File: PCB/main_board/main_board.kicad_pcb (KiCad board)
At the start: 4 copper layers, 57 x 29 mm, 55 parts, among them CN1 XT30PW-M, CN2 XT30PW-M, U1 XT30PW-F, U2 W25Q32JVUUIQ, U3 W25N01GVZEIG_C907680, U4 INA226, U5 INA226, U6 RP2040, U7 AZ1117-3.3, X1 X322512MSB4SI

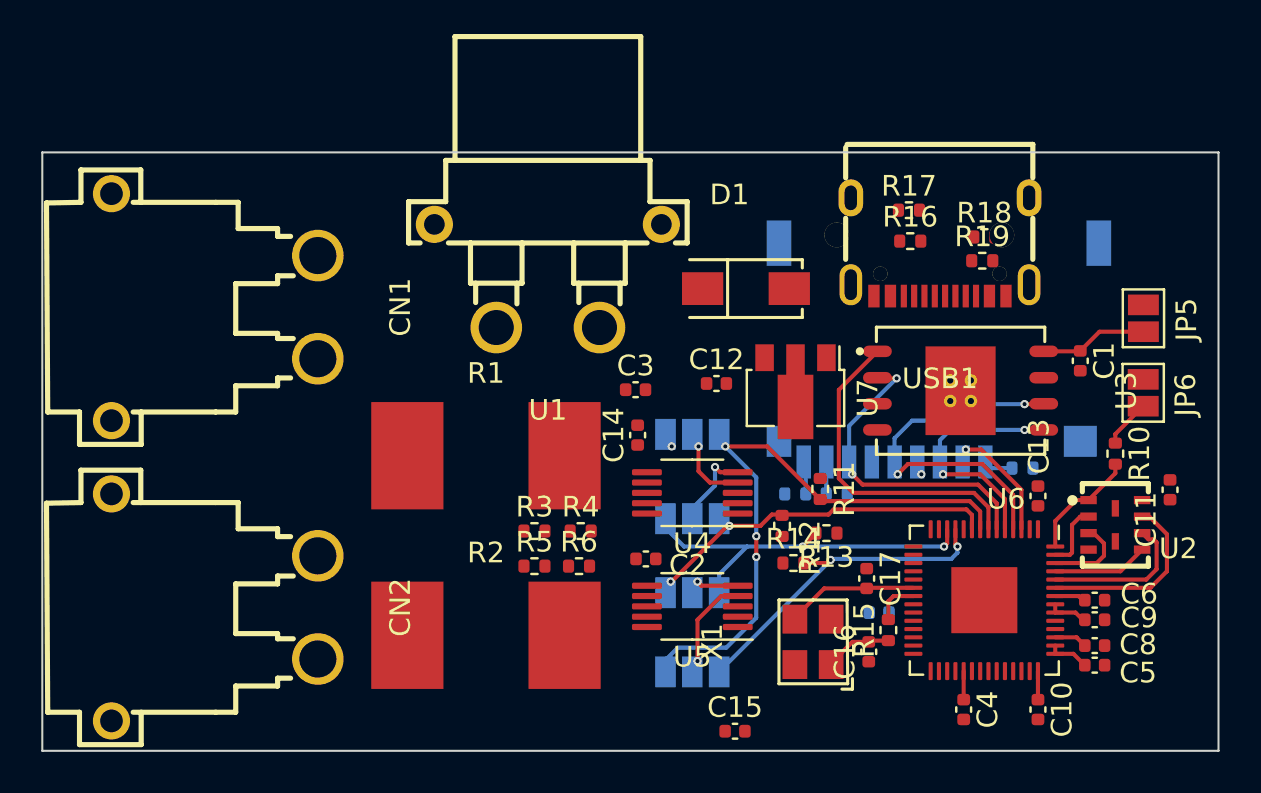
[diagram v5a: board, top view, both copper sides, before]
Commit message: Complete high current trace
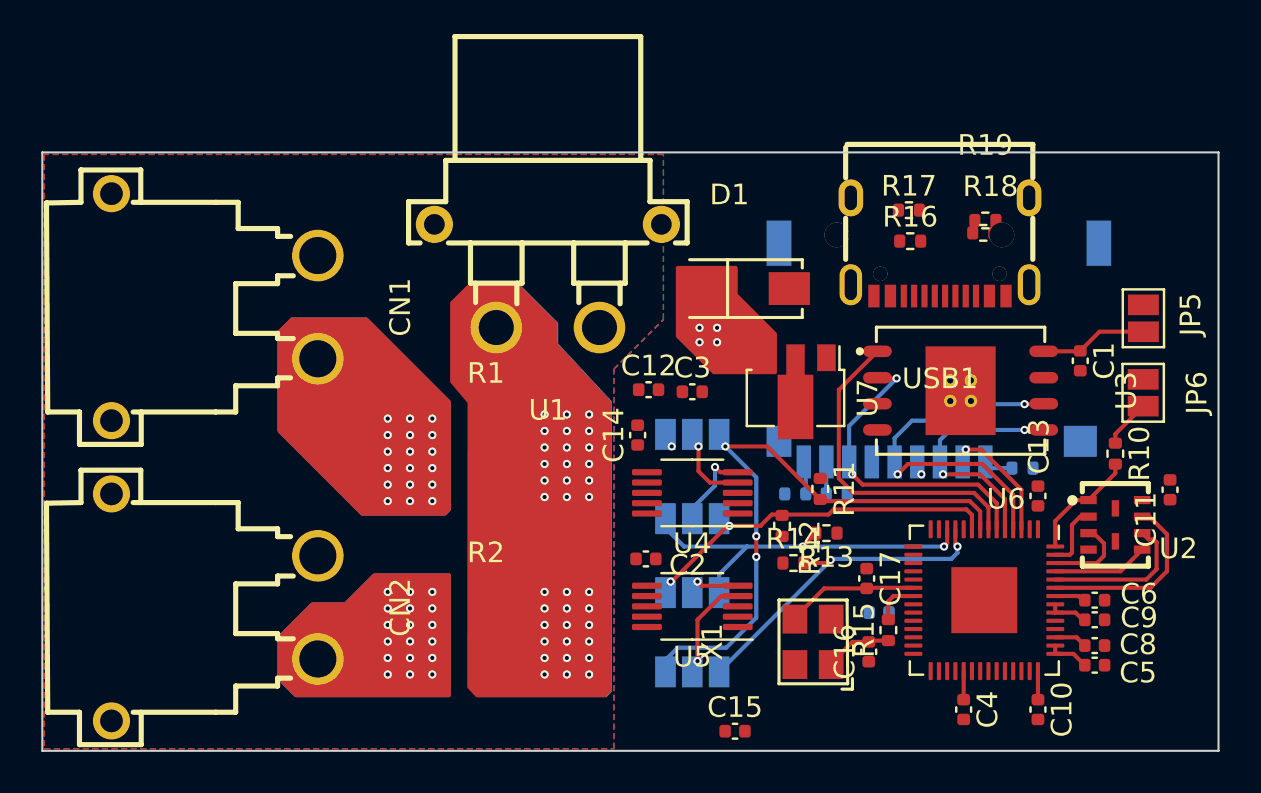
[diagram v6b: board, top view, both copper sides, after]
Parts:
- removed R3, R4, R5, R6: 10, Resistor_SMD:R_0402_1005Metric
- moved C12 3.30 mm to (54.9, 36.0)
- moved C3 2.75 mm to (57.0, 36.1)
- moved R19 1.35 mm to (71.1, 28.4)
- moved R18 0.80 mm to (71.2, 27.8)
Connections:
- CN1 pad 3: unconnected-(CN1-Pad3) -> GND
- CN1 pad 4: unconnected-(CN1-Pad4) -> GND
- CN2 pad 3: unconnected-(CN2-Pad3) -> GND
- CN2 pad 4: unconnected-(CN2-Pad4) -> GND
- U1 pad 3: unconnected-(U1-Pad3) -> GND
- U1 pad 4: unconnected-(U1-Pad4) -> GND
- U4 pad 10: Net-(U4-Vin+) -> IBAT+
- U4 pad 9: Net-(U4-Vin-) -> IBAT-
- U5 pad 10: Net-(U5-Vin+) -> ICAP+
- U5 pad 9: Net-(U5-Vin-) -> IBAT-
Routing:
- net IBAT+: track 0.00 -> 19.7 mm, vias 0 -> 22
- net ICAP+: vias 0 -> 18
- net IBAT-: vias 0 -> 36
- added copper zone on B.Cu, net GND
- added copper zone on F.Cu, net GND

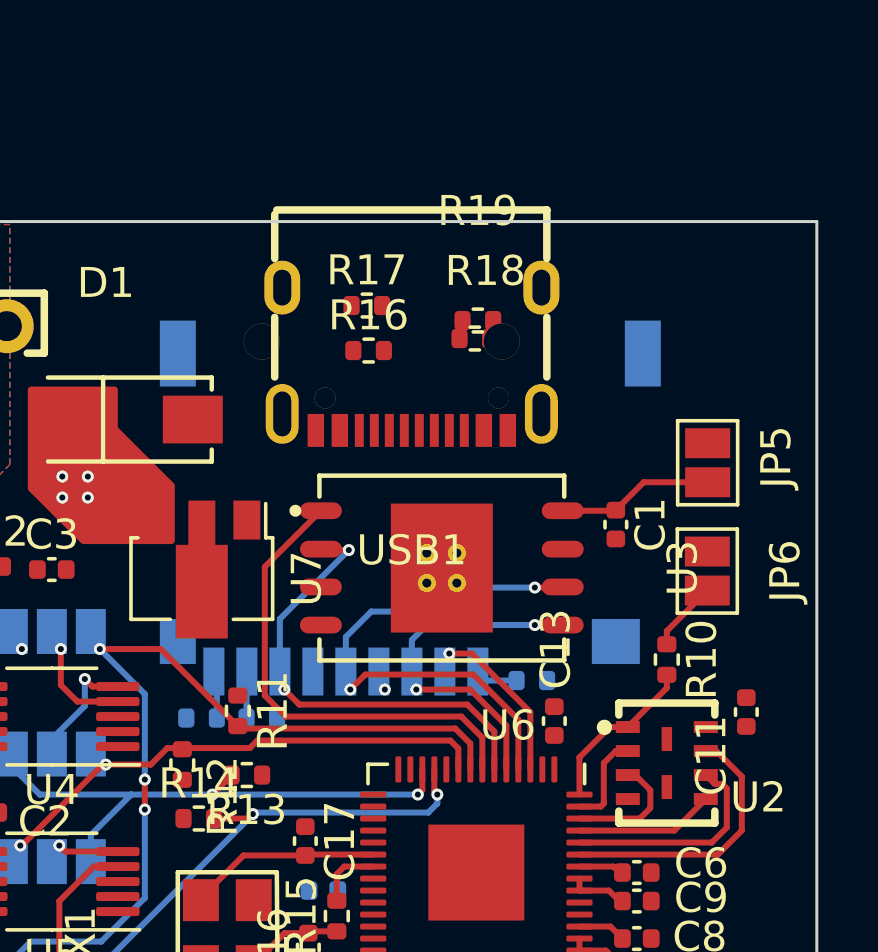
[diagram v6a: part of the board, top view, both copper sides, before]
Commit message: Complete VBUS trace; Adjust Flash position
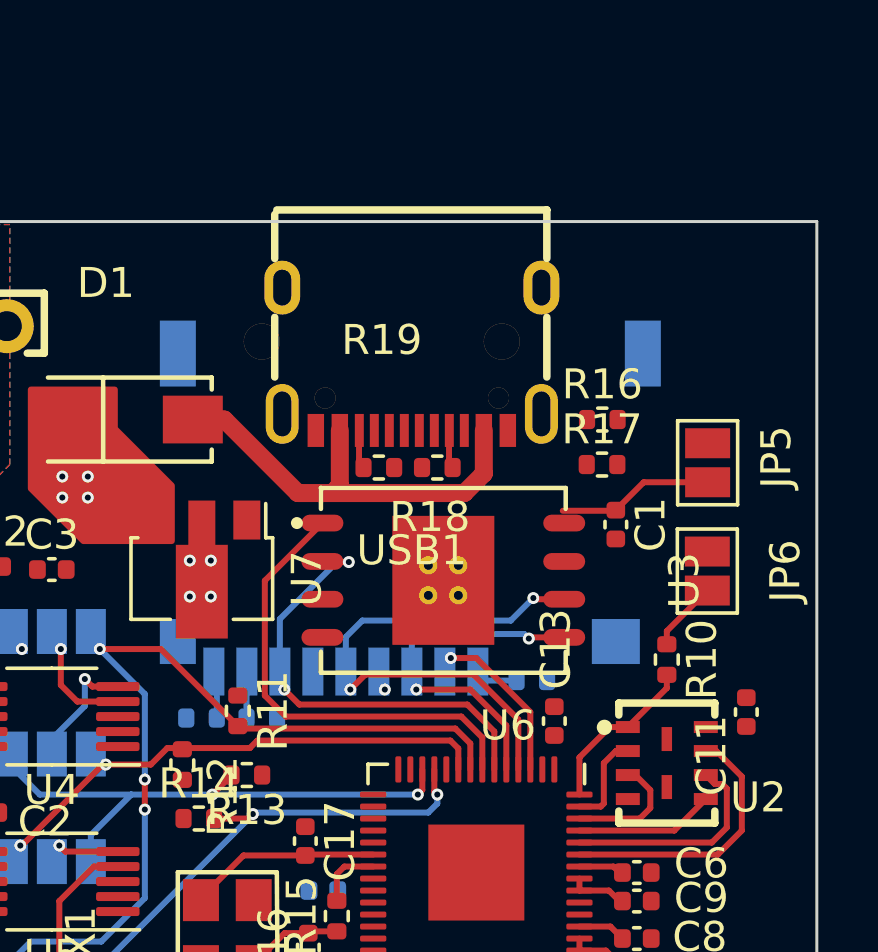
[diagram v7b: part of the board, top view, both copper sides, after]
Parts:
- moved R17 9.46 mm to (75.3, 32.6)
- moved R16 8.12 mm to (75.3, 31.1)
- moved R19 5.36 mm to (67.9, 32.7)
- moved R18 5.08 mm to (69.8, 32.7), turned to 180 degrees
- moved U3 0.41 mm to (70.0, 36.5)
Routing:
- net VBUS: track 0.00 -> 14.6 mm
- net Net-(USB1-CC2): track 0.00 -> 1.09 mm
- net Net-(USB1-CC1): track 0.00 -> 1.04 mm
- net +3.3V: vias 1 -> 5

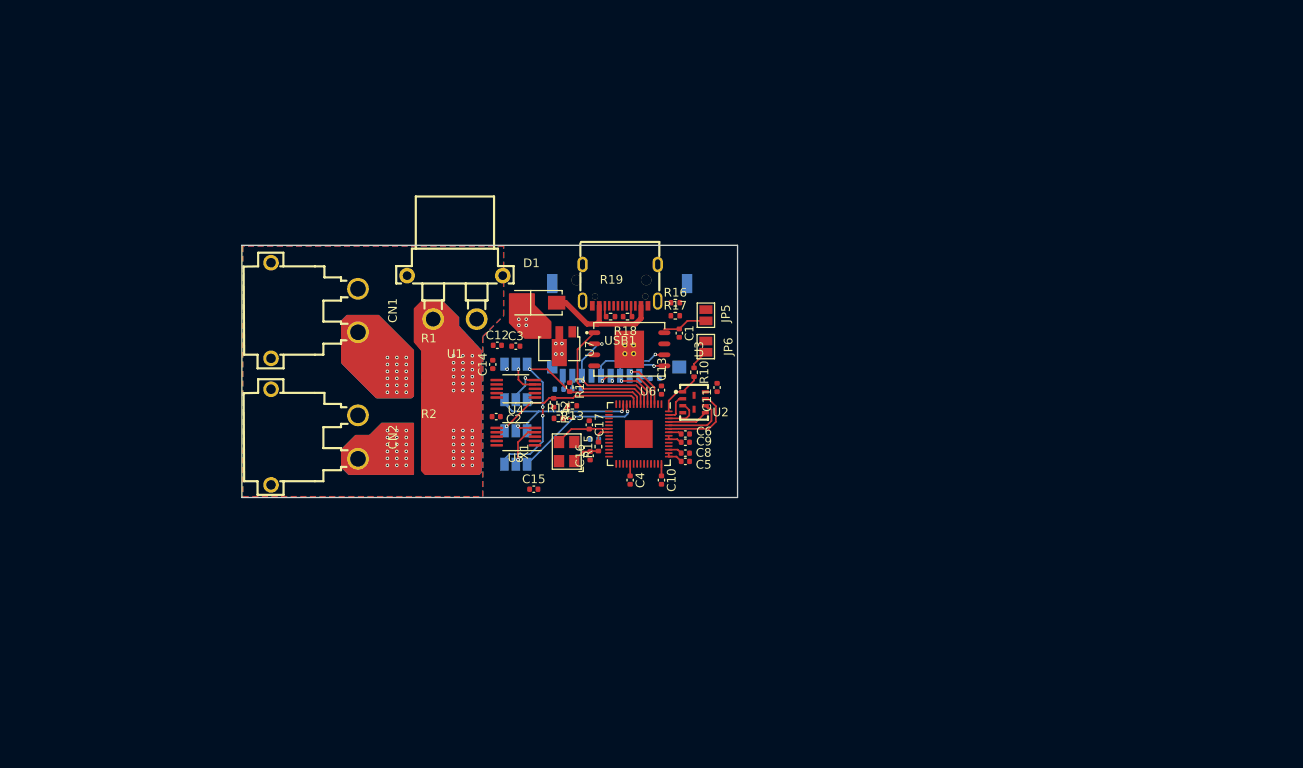
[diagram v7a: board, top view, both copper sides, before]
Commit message: Complete USB DP routing
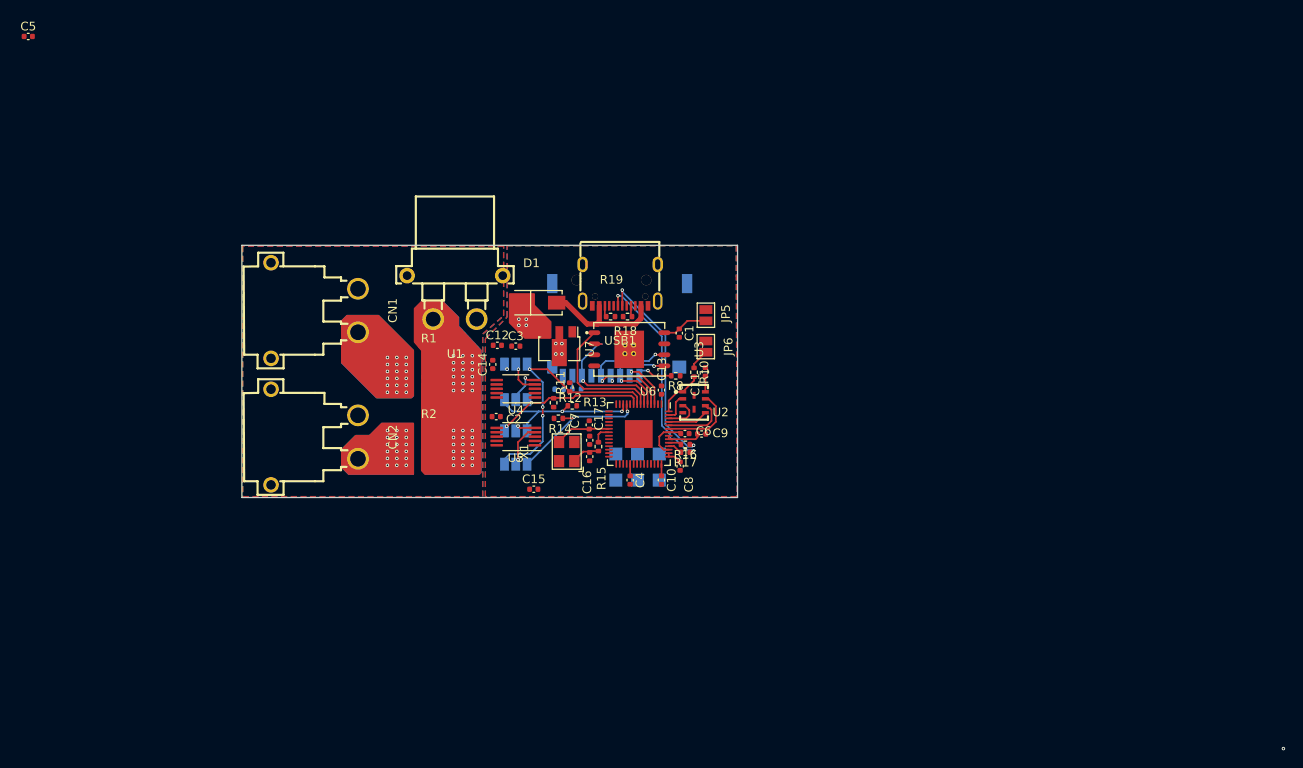
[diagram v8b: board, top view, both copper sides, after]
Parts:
- added TP1: SWCLK, TestPoint:TestPoint_Pad_1.5x1.5mm, B.Cu at (73.5, 51.5)
- added TP2: SWD, TestPoint:TestPoint_Pad_1.5x1.5mm, B.Cu at (71.0, 51.5)
- added TP3: UART0 TX, TestPoint:TestPoint_Pad_1.5x1.5mm, B.Cu at (73.5, 48.5)
- added TP4: UART0 RX, TestPoint:TestPoint_Pad_1.5x1.5mm, B.Cu at (71.0, 48.5)
- added TP5: GND, TestPoint:TestPoint_Pad_1.5x1.5mm, B.Cu at (68.5, 51.5)
- added TP6: GND, TestPoint:TestPoint_Pad_1.5x1.5mm, B.Cu at (68.5, 48.5)
- C7, R8: moved to F.Cu
- moved C5 89.5 mm to (0.94, 0.48), turned to 0 degrees
- moved R16 16.3 mm to (76.5, 47.4), turned to 180 degrees
- moved R17 15.7 mm to (76.5, 48.3), turned to 180 degrees
- moved R8 2.41 mm to (75.4, 39.5)
- moved C11 2.25 mm to (78.8, 39.0)
- moved C9 2.10 mm to (78.4, 46.2)
- moved C8 0.81 mm to (75.9, 49.9), turned to -90 degrees
- moved C7 0.56 mm to (65.5, 46.9), turned to -90 degrees
- moved C16 0.11 mm to (65.5, 48.8)
- moved C6 0.07 mm to (76.5, 46.1)
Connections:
- net Net-(USB1-DN1) renamed USB+
- net Net-(USB1-DP1) renamed USB-
- Card1 pad 10: unconnected-(Card1-EP-Pad10) -> GND
- Card1 pad 11: unconnected-(Card1-EP-Pad11) -> GND
- Card1 pad 12: unconnected-(Card1-EP-Pad12) -> GND
- Card1 pad 13: unconnected-(Card1-EP-Pad13) -> GND
- U3 pad 9: unconnected-(U3-EP-Pad9) -> GND
- U6 pad 24: unconnected-(U6-SWCLK-Pad24) -> Net-(U6-SWCLK)
- U6 pad 25: unconnected-(U6-SWD-Pad25) -> Net-(U6-SWD)
- U6 pad 28: unconnected-(U6-GPIO17-Pad28) -> /TX0
- U6 pad 29: unconnected-(U6-GPIO18-Pad29) -> /RX0
- USB1 pad 13: unconnected-(USB1-SHELL-Pad13) -> GND
- USB1 pad 14: unconnected-(USB1-SHELL-Pad14) -> GND
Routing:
- net USB-: track 0.00 -> 24.1 mm, vias 0 -> 2
- net USB+: track 0.00 -> 24.1 mm, vias 0 -> 2
- net +3.3V: track 6.84 -> 10.7 mm
- net Net-(Card1-DAT2): track 1.41 -> 4.81 mm, vias 0 -> 1
- net +1V1: track 3.15 -> 5.15 mm
- net Net-(U6-USB_DM): track 0.00 -> 1.80 mm
- net Net-(U6-USB_DP): track 0.00 -> 1.49 mm
- added copper zone on In2.Cu, net GND
